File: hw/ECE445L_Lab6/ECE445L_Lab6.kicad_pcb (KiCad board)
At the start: 2 copper layers, 114.4 x 88.9 mm, 32 parts, among them J1 JTAG, J2 Battery, SW1 Reset, SW2 Input, U1 TM4C123GH6PMIR, U2 Adafruit ST7735R, U3 LP2950-33LPRE3, Y1 ABM3-16.000MHZ-B2-T

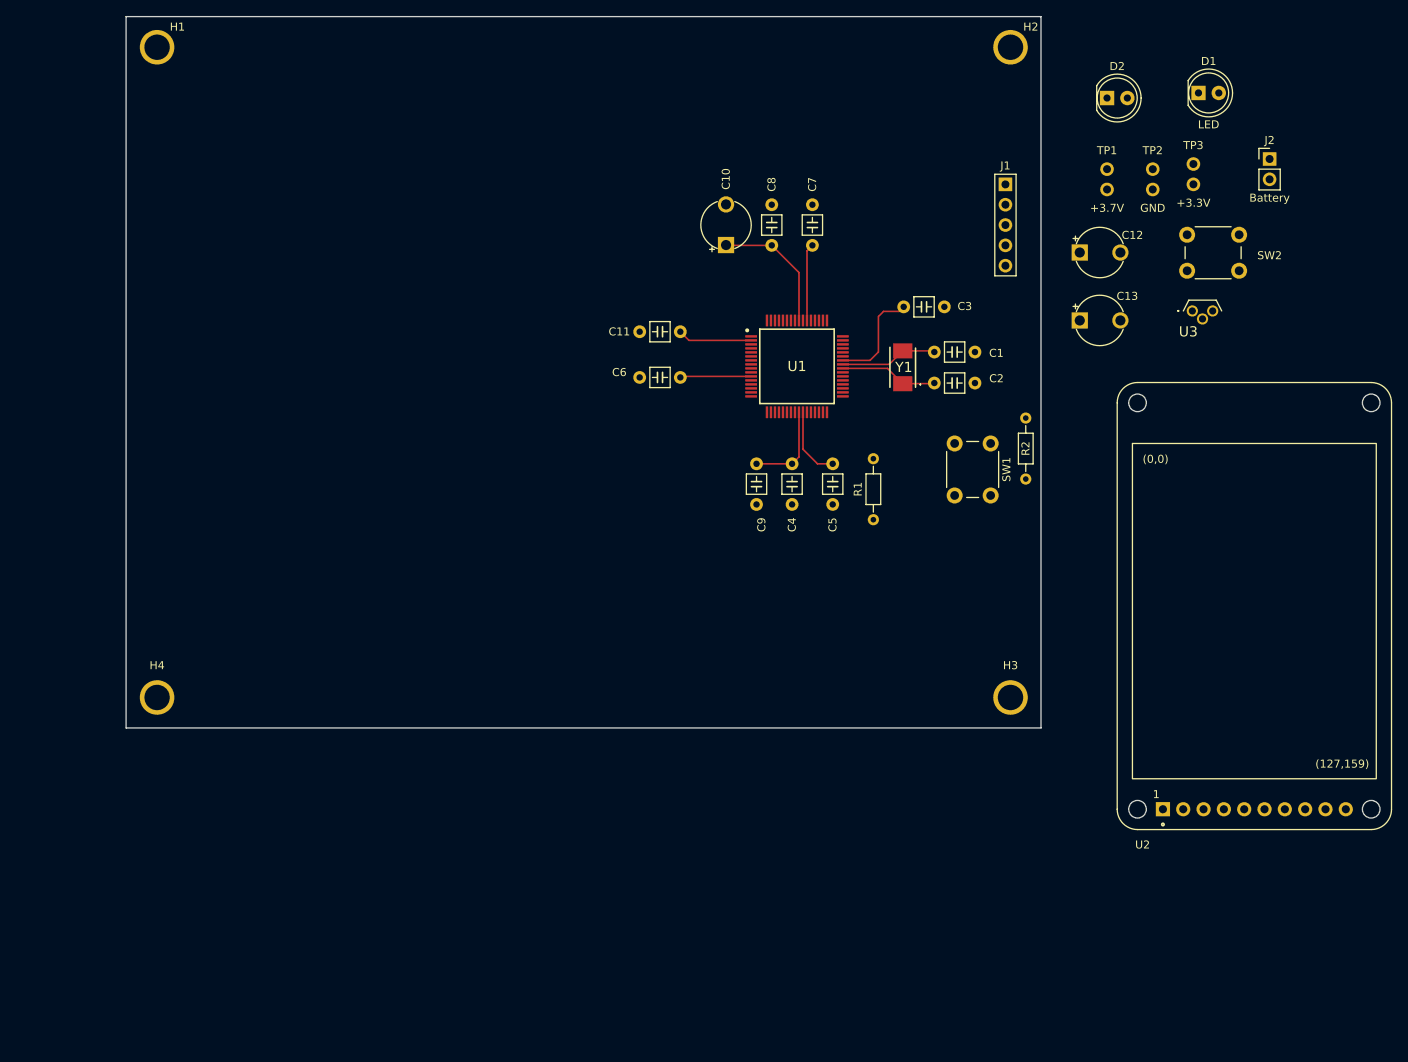
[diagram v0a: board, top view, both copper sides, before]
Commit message: all hardware changes
fully updated schematic and pcb, most of changes were local to prevent corrupting files when pulling.
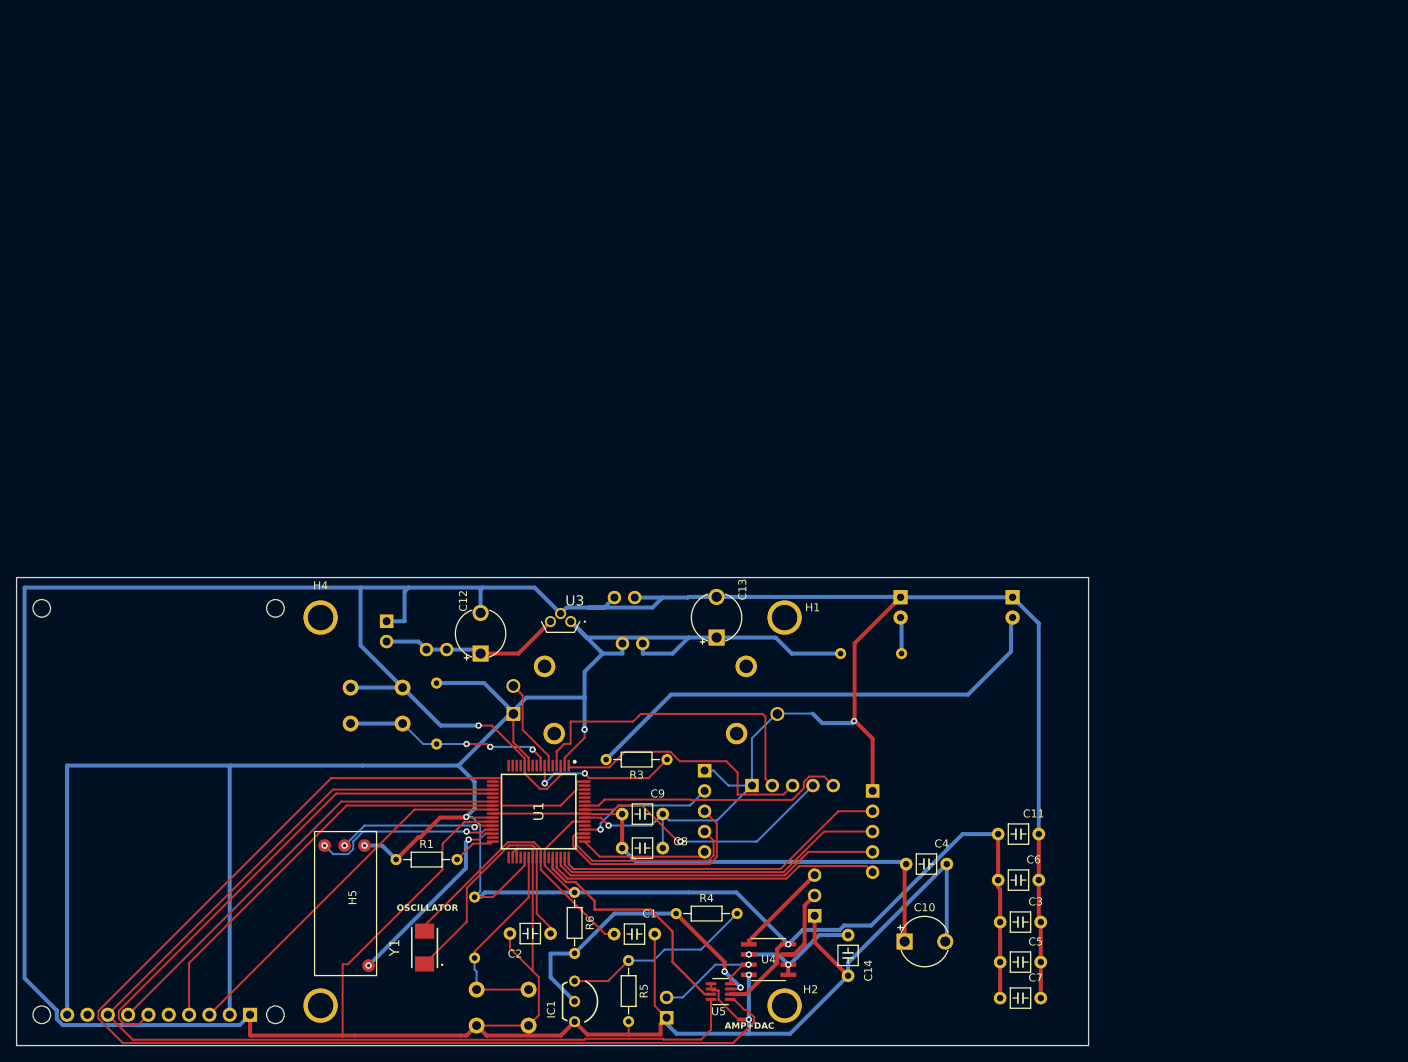
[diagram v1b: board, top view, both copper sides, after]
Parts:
- added C14: 1uF, ECE445L:C_Axial_200mil, F.Cu at (121.9, 140.2)
- added H5: ~, Lab_6:HEARTBEAT, F.Cu at (39.5, 147.8)
- added IC1: LM4041CILPR, ECE445L:ti_LM4041CILPR, F.Cu at (87.8, 148.5)
- added J4: LOGIC_0-3, ECE445L:PinHeader_1x05_P2.54mm_Vertical, B.Cu at (125.0, 122.2)
- added J5: LOGIC_4-7, ECE445L:PinHeader_1x05_P2.54mm_Vertical, B.Cu at (109.9, 121.5)
- added J7: DAC_Test, ECE445L:PinHeader_1x02_P2.54mm_Vertical, B.Cu at (99.2, 150.5)
- added J8: Header3, ECE445L:PinHeader_1x03_P2.54mm_Vertical, B.Cu at (117.8, 137.8)
- added R3: 10k, ECE445L:R_Axial_DIN0204_L3.6mm_D1.6mm_P7.62mm_Horizontal, F.Cu at (99.3, 118.2)
- added R4: 3.3k, ECE445L:R_Axial_DIN0204_L3.6mm_D1.6mm_P7.62mm_Horizontal, F.Cu at (100.4, 137.5)
- added R5: 10k, ECE445L:R_Axial_DIN0204_L3.6mm_D1.6mm_P7.62mm_Horizontal, F.Cu at (94.5, 143.4)
- added R6: 9k, ECE445L:R_Axial_DIN0204_L3.6mm_D1.6mm_P7.62mm_Horizontal, F.Cu at (87.8, 134.9)
- added R7: 10k, ECE445L:R_Axial_DIN0204_L3.6mm_D1.6mm_P7.62mm_Horizontal, B.Cu at (70.5, 108.7)
- added R8: 10k, ECE445L:R_Axial_DIN0204_L3.6mm_D1.6mm_P7.62mm_Horizontal, B.Cu at (121.0, 105.0)
- added RV1: PTA2043, ECE445L:PTA2043pot, B.Cu at (80.1, 112.5)
- added U4: AD822ARZ, Lab_6:R_8_ADI, F.Cu at (112.0, 143.2)
- added U5: AD5061BRJZ-1500RL7, Lab_6:RJ_8_ADI, F.Cu at (106.0, 147.2)
- D1, D2, J1, J2, R2, SW1, SW2, TP1, TP2, TP3, U2: moved to B.Cu
- moved U2 139.4 mm to (35.8, 124.8), turned to 180 degrees
- moved J2 124.6 mm to (64.2, 101.0), turned to 180 degrees
- moved H2 123.1 mm to (114.0, 149.0)
- moved SW2 113.2 mm to (66.2, 109.2), turned to 180 degrees
- moved H1 106.0 mm to (114.0, 100.5)
- moved TP1 104.1 mm to (69.2, 104.5), turned to -90 degrees
- moved SW1 97.1 mm to (75.5, 151.5), turned to 0 degrees
- moved C7 97.0 mm to (140.9, 148.1), turned to 0 degrees
- moved H3 94.4 mm to (56.0, 149.0)
- moved Y1 94.0 mm to (69.0, 141.8)
- moved TP3 93.2 mm to (93.7, 103.8), turned to -90 degrees
- moved R2 91.3 mm to (75.2, 135.4)
- moved C12 90.1 mm to (76.0, 105.0), turned to 90 degrees
- moved C10 89.9 mm to (129.0, 141.0), turned to 0 degrees
- moved U3 86.9 mm to (87.3, 101.0), turned to 180 degrees
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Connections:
- D1 pad 1: unconnected-(D1-K-Pad1) -> GND
- D1 pad 2: unconnected-(D1-A-Pad2) -> Net-(D1-A)
- D2 pad 1: unconnected-(D2-K-Pad1) -> GND
- D2 pad 2: unconnected-(D2-A-Pad2) -> Net-(D2-A)
- SW2 pad 1: unconnected-(SW2-Pad1) -> GND
- SW2 pad 2: unconnected-(SW2-Pad2) -> PE1
- U1 pad 10: PD7 -> unconnected-(U1-PD7-Pad10)
- U1 pad 13: PC7 -> unconnected-(U1-PC7-Pad13)
- U1 pad 14: PC6 -> unconnected-(U1-PC6-Pad14)
- U1 pad 15: PC5 -> unconnected-(U1-PC5-Pad15)
- U1 pad 16: PC4 -> unconnected-(U1-PC4-Pad16)
- U1 pad 17: PA0 -> unconnected-(U1-PA0/U0RX-Pad17)
- U1 pad 18: PA1 -> unconnected-(U1-PA1/U0TX-Pad18)
- U1 pad 21: PA4 -> unconnected-(U1-PA4/SSI0RX-Pad21)
- U1 pad 28: PF0 -> Net-(H5-LED_Brightness)
- U1 pad 29: PF1 -> Net-(H5-GND)
- U1 pad 30: PF2 -> Net-(H5-Vout)
- U1 pad 31: PF3 -> unconnected-(U1-PF3-Pad31)
- U1 pad 43: PD4 -> unconnected-(U1-PD4-Pad43)
- U1 pad 5: PF4 -> unconnected-(U1-PF4-Pad5)
- U1 pad 53: PD6 -> unconnected-(U1-PD6-Pad53)
- U1 pad 59: PE4 -> unconnected-(U1-PE4-Pad59)
- U1 pad 60: PE5 -> unconnected-(U1-PE5-Pad60)
- U1 pad 61: PD0 -> unconnected-(U1-PD0-Pad61)
- U1 pad 62: PD1 -> unconnected-(U1-PD1-Pad62)
- U1 pad 63: PD2 -> unconnected-(U1-PD2-Pad63)
- U1 pad 9: PE0 -> unconnected-(U1-PE0-Pad9)
- U2 pad 1: unconnected-(U2-GND-Pad1) -> GND
- U2 pad 10: unconnected-(U2-LITE-Pad10) -> +3V3
- U2 pad 2: unconnected-(U2-VCC-Pad2) -> +3V3
- U2 pad 3: unconnected-(U2-RESET-Pad3) -> PA7
- U2 pad 4: unconnected-(U2-D/C-Pad4) -> PA6
- U2 pad 6: unconnected-(U2-TFT_CS-Pad6) -> PA3
- U2 pad 7: unconnected-(U2-MOSI-Pad7) -> PA5
- U2 pad 8: unconnected-(U2-SCK-Pad8) -> PA2
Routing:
- net GND: track 0.00 -> 636.5 mm, vias 0 -> 5
- net +3V3: track 49.9 -> 384.0 mm, vias 0 -> 4
- net PD3: track 0.00 -> 167.8 mm
- net PA2: track 0.00 -> 140.9 mm
- net PA3: track 0.00 -> 63.4 mm
- net Net-(D1-A): track 0.00 -> 60.5 mm
- net PA5: track 0.00 -> 56.6 mm
- net PA6: track 0.00 -> 52.6 mm
- net PA7: track 0.00 -> 46.0 mm
- net PB0: track 0.00 -> 42.3 mm
- net PB3: track 0.00 -> 42.1 mm
- net PB2: track 0.00 -> 41.9 mm
- net PB1: track 0.00 -> 41.7 mm
- net PB7: track 0.00 -> 40.5 mm
- net Net-(U5-VREF): track 0.00 -> 39.0 mm, vias 0 -> 2
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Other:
- board size 114.4 x 88.9 mm -> 134 x 58.5 mm
- board text added: "AMP+DAC"
- board text added: "HEARTBEAT"
- board text added: "LCD SCREEN"
- board text added: "MODE SWITCH"
- board text added: "ON LED"
- board text added: "OSCILLATOR"
- board text added: "RESET"
